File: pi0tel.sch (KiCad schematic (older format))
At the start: 3 parts

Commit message: hmmm
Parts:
- added C1: 680uF, Capacitor_SMD:C_1206_3216Metric_Pad1.42x1.75mm_HandSolder, symbol Device:CP
- added C2: 220uF, Capacitor_SMD:C_1206_3216Metric_Pad1.42x1.75mm_HandSolder, symbol Device:CP
- added D1: Schottky 3A, Diode_SMD:D_1206_3216Metric_Pad1.42x1.75mm_HandSolder, symbol Device:D_Schottky
- added J1: DIN-5_180degree, footprints:din_5_econet_pcb_mount, symbol Connector:DIN-5_180degree
- added J2: RPi_GPIO, Connector_PinHeader_2.54mm:PinHeader_2x20_P2.54mm_Vertical, symbol Connector-ML:RPi_GPIO
- added L1: 33uH, Inductor_SMD:L_12x12mm_H6mm, symbol Device:L
- added U1: LM2596S-5, Package_TO_SOT_SMD:TO-263-5_TabPin3, symbol Regulator_Switching:LM2596S-5
- gave numbers to parts that had none: 2
- renumbered 10k to 10k1
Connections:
- net labels added: GND
- wire segments 13 -> 36
- no-connect marks 0 -> 36
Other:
- note added: "Thru-Hole Connector"
- moved on the sheet: 10k1, Q1, R1

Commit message: grrr
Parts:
- J1: footprint footprints:din_5_econet_pcb_mount -> myelin-kicad:din_5_econet_pcb_mount
- R2: renamed from 10k1; value R -> 10k
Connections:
- net GND: no longer C1.1, J1.5, U1.1 (VIN)
- new net MinitelVcc: C1.1, J1.5, U1.1 (VIN)
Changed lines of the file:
@@
 EESchema Schematic File Version 4
 LIBS:pi0tel-cache
-LIBS:RPi_Zero_pHat_Template-cache
 EELAYER 26 0
 EELAYER END
@@
 $EndComp
 $Comp
-L Device:R 10k1
+L Device:R R2
 U 1 1 5EFD4A91
 P 3200 2600
-F 0 "10k1" H 3270 2646 50  0000 L CNN
-F 1 "R" H 3270 2555 50  0000 L CNN
+F 0 "R2" H 3270 2646 50  0000 L CNN
+F 1 "10k" H 3270 2555 50  0000 L CNN
 F 2 "Resistor_SMD:R_0805_2012Metric_Pad1.15x1.40mm_HandSolder" V 3130 2600 50  0001 C CNN
 F 3 "~" H 3200 2600 50  0001 C CNN
@@
 	1350 4300 1650 4300
 Wire Wire Line
-	1350 4300 1350 4900
-Wire Wire Line
-	1350 4900 1650 4900
-Wire Wire Line
 	2750 4900 2750 4700
-Connection ~ 1350 4300
 Wire Wire Line
 	1650 4750 1650 4900
-Connection ~ 1650 4900
 Wire Wire Line
 	1650 4900 2250 4900
@@
 Wire Wire Line
 	4850 4300 4850 4500
-Text Label 1350 4000 0    50   ~ 0
+Text Label 1350 4300 0    50   ~ 0
 MinitelVcc
-Wire Wire Line
-	1350 4000 1350 4300
 $Comp
 L Connector:DIN-5_180degree J1
@@
 F 0 "J1" H 5500 2526 50  0000 C CNN
 F 1 "DIN-5_180degree" H 5500 2435 50  0000 C CNN
-F 2 "footprints:din_5_econet_pcb_mount" H 5500 2800 50  0001 C CNN
+F 2 "myelin-kicad:din_5_econet_pcb_mount" H 5500 2800 50  0001 C CNN
 F 3 "http://www.mouser.com/ds/2/18/40_c091_abd_e-75918.pdf" H 5500 2800 50  0001 C CNN
 	1    5500 2800

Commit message: hmmm
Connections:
- net +3V3: now also J2.17 (3.3V); no longer J2.1 (3.3V)
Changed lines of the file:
@@
 NoConn ~ 7300 3300
 NoConn ~ 7300 3400
-NoConn ~ 7300 3500
+NoConn ~ 7300 2700
 NoConn ~ 7300 3600
 NoConn ~ 7300 3700
@@
 L power:+3.3V #PWR0107
 U 1 1 5EFA719F
-P 7300 2700
-F 0 "#PWR0107" H 7300 2550 50  0001 C CNN
-F 1 "+3.3V" V 7315 2828 50  0000 L CNN
-F 2 "" H 7300 2700 50  0001 C CNN
-F 3 "" H 7300 2700 50  0001 C CNN
-	1    7300 2700
+P 7300 3500
+F 0 "#PWR0107" H 7300 3350 50  0001 C CNN
+F 1 "+3.3V" V 7315 3628 50  0000 L CNN
+F 2 "" H 7300 3500 50  0001 C CNN
+F 3 "" H 7300 3500 50  0001 C CNN
+	1    7300 3500
 	0    -1   -1   0
 $EndComp

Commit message: getting there
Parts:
- C1: value 680uF -> 270uF; footprint Capacitor_SMD:C_1206_3216Metric_Pad1.42x1.75mm_HandSolder -> Capacitor_SMD:CP_Elec_8x10.5
- C2: value 220uF -> 470uF; footprint Capacitor_SMD:C_1206_3216Metric_Pad1.42x1.75mm_HandSolder -> Capacitor_SMD:CP_Elec_8x10.5
- L1: value 33uH -> 68uH
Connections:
- net +5V: now also J2.4 (5V)
- net GND: now also J2.9 (GND); no longer J2.25 (GND)
- no-connect marks 36 -> 35
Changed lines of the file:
@@
 P 4350 4500
 F 0 "L1" V 4172 4500 50  0000 C CNN
-F 1 "33uH" V 4263 4500 50  0000 C CNN
+F 1 "68uH" V 4263 4500 50  0000 C CNN
 F 2 "Inductor_SMD:L_12x12mm_H6mm" H 4350 4500 50  0001 C CNN
 F 3 "~" H 4350 4500 50  0001 C CNN
@@
 P 1650 4600
 F 0 "C1" H 1768 4646 50  0000 L CNN
-F 1 "680uF" H 1768 4555 50  0000 L CNN
-F 2 "Capacitor_SMD:C_1206_3216Metric_Pad1.42x1.75mm_HandSolder" H 1688 4450 50  0001 C CNN
+F 1 "270uF" H 1768 4555 50  0000 L CNN
+F 2 "Capacitor_SMD:CP_Elec_8x10.5" H 1688 4450 50  0001 C CNN
 F 3 "~" H 1650 4600 50  0001 C CNN
 	1    1650 4600
@@
 P 4850 4700
 F 0 "C2" H 4968 4746 50  0000 L CNN
-F 1 "220uF" H 4968 4655 50  0000 L CNN
-F 2 "Capacitor_SMD:C_1206_3216Metric_Pad1.42x1.75mm_HandSolder" H 4888 4550 50  0001 C CNN
+F 1 "470uF" H 4968 4655 50  0000 L CNN
+F 2 "Capacitor_SMD:CP_Elec_8x10.5" H 4888 4550 50  0001 C CNN
 F 3 "~" H 4850 4700 50  0001 C CNN
 	1    4850 4700
@@
 NoConn ~ 7300 2800
 NoConn ~ 7300 2900
-NoConn ~ 7300 3100
+NoConn ~ 7300 3900
 NoConn ~ 7300 3200
 NoConn ~ 7300 3300
@@
 NoConn ~ 9200 3200
 NoConn ~ 9200 2900
-NoConn ~ 9200 2800
 $Comp
 L power:+5V #PWR0106
@@
 L power:GND #PWR0108
 U 1 1 5EFA81A2
-P 7300 3900
-F 0 "#PWR0108" H 7300 3650 50  0001 C CNN
-F 1 "GND" V 7305 3772 50  0000 R CNN
-F 2 "" H 7300 3900 50  0001 C CNN
-F 3 "" H 7300 3900 50  0001 C CNN
-	1    7300 3900
+P 7300 3100
+F 0 "#PWR0108" H 7300 2850 50  0001 C CNN
+F 1 "GND" V 7305 2972 50  0000 R CNN
+F 2 "" H 7300 3100 50  0001 C CNN
+F 3 "" H 7300 3100 50  0001 C CNN
+	1    7300 3100
 	0    1    1    0
 $EndComp
@@
 Text Label 5800 2700 0    50   ~ 0
 MinitelVcc
+$Comp
+L power:+5V #PWR?
+U 1 1 5EFBBFDE
+P 9200 2800
+F 0 "#PWR?" H 9200 2650 50  0001 C CNN
+F 1 "+5V" V 9215 2928 50  0000 L CNN
+F 2 "" H 9200 2800 50  0001 C CNN
+F 3 "" H 9200 2800 50  0001 C CNN
+	1    9200 2800
+	0    1    1    0
+$EndComp
 $EndSCHEMATC

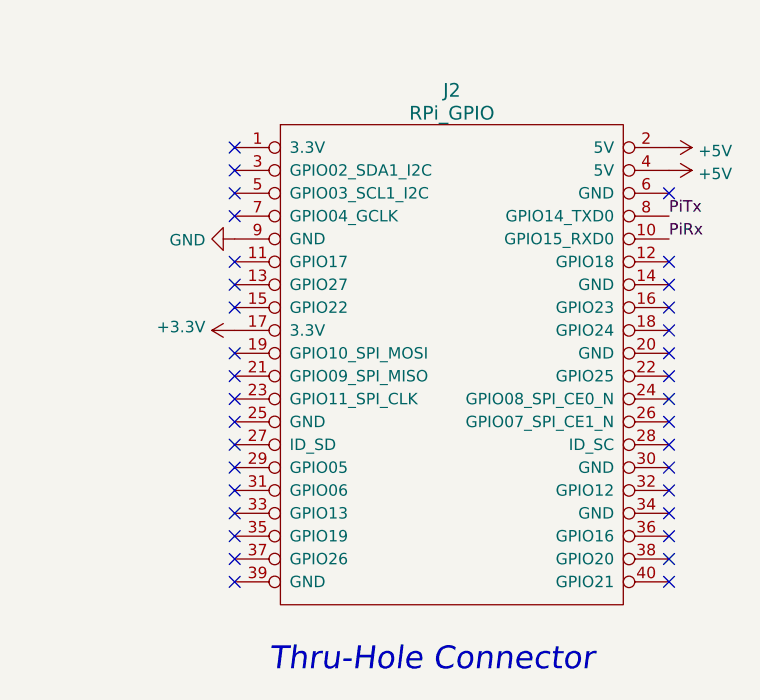
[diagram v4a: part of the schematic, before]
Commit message: Move din to the back
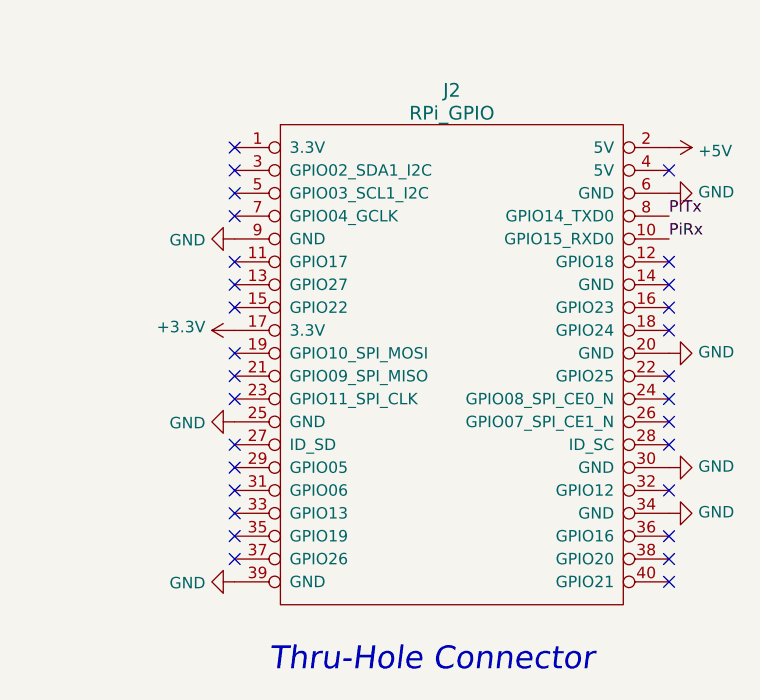
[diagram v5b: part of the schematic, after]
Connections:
- net +5V: no longer J2.4 (5V)
- net GND: now also J2.20 (GND), J2.25 (GND), J2.30 (GND), J2.34 (GND), J2.39 (GND), J2.6 (GND)
- no-connect marks 35 -> 30
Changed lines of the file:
@@
 NoConn ~ 7300 2800
 NoConn ~ 7300 2900
-NoConn ~ 7300 3900
 NoConn ~ 7300 3200
 NoConn ~ 7300 3300
@@
 NoConn ~ 7300 4400
 NoConn ~ 7300 4500
-NoConn ~ 7300 4600
 NoConn ~ 9200 4600
 NoConn ~ 9200 4500
 NoConn ~ 9200 4400
-NoConn ~ 9200 4300
 NoConn ~ 9200 4200
-NoConn ~ 9200 4100
 NoConn ~ 9200 4000
 NoConn ~ 9200 3900
 NoConn ~ 9200 3800
 NoConn ~ 9200 3700
-NoConn ~ 9200 3600
 NoConn ~ 9200 3500
 NoConn ~ 9200 3400
 NoConn ~ 9200 3300
 NoConn ~ 9200 3200
-NoConn ~ 9200 2900
 $Comp
 L power:+5V #PWR0106
@@
 Text Label 5800 2700 0    50   ~ 0
 MinitelVcc
+NoConn ~ 9200 2800
 $Comp
-L power:+5V #PWR?
-U 1 1 5EFBBFDE
-P 9200 2800
-F 0 "#PWR?" H 9200 2650 50  0001 C CNN
-F 1 "+5V" V 9215 2928 50  0000 L CNN
-F 2 "" H 9200 2800 50  0001 C CNN
-F 3 "" H 9200 2800 50  0001 C CNN
-	1    9200 2800
+L power:GND #PWR?
+U 1 1 5EFCD1E8
+P 7300 3900
+F 0 "#PWR?" H 7300 3650 50  0001 C CNN
+F 1 "GND" V 7305 3772 50  0000 R CNN
+F 2 "" H 7300 3900 50  0001 C CNN
+F 3 "" H 7300 3900 50  0001 C CNN
+	1    7300 3900
 	0    1    1    0
 $EndComp
+$Comp
+L power:GND #PWR?
+U 1 1 5EFCD6C1
+P 7300 4600
+F 0 "#PWR?" H 7300 4350 50  0001 C CNN
+F 1 "GND" V 7305 4472 50  0000 R CNN
+F 2 "" H 7300 4600 50  0001 C CNN
+F 3 "" H 7300 4600 50  0001 C CNN
+	1    7300 4600
+	0    1    1    0
+$EndComp
+$Comp
+L power:GND #PWR?
+U 1 1 5EFCE70C
+P 9200 3600
+F 0 "#PWR?" H 9200 3350 50  0001 C CNN
+F 1 "GND" V 9205 3472 50  0000 R CNN
+F 2 "" H 9200 3600 50  0001 C CNN
+F 3 "" H 9200 3600 50  0001 C CNN
+	1    9200 3600
+	0    -1   -1   0
+$EndComp
+$Comp
+L power:GND #PWR?
+U 1 1 5EFCEF5F
+P 9200 4100
+F 0 "#PWR?" H 9200 3850 50  0001 C CNN
+F 1 "GND" V 9205 3972 50  0000 R CNN
+F 2 "" H 9200 4100 50  0001 C CNN
+F 3 "" H 9200 4100 50  0001 C CNN
+	1    9200 4100
+	0    -1   -1   0
+$EndComp
+$Comp
+L power:GND #PWR?
+U 1 1 5EFCEF7E
+P 9200 4300
+F 0 "#PWR?" H 9200 4050 50  0001 C CNN
+F 1 "GND" V 9205 4172 50  0000 R CNN
+F 2 "" H 9200 4300 50  0001 C CNN
+F 3 "" H 9200 4300 50  0001 C CNN
+	1    9200 4300
+	0    -1   -1   0
+$EndComp
+$Comp
+L power:GND #PWR?
+U 1 1 5EFCEFA7
+P 9200 2900
+F 0 "#PWR?" H 9200 2650 50  0001 C CNN
+F 1 "GND" V 9205 2772 50  0000 R CNN
+F 2 "" H 9200 2900 50  0001 C CNN
+F 3 "" H 9200 2900 50  0001 C CNN
+	1    9200 2900
+	0    -1   -1   0
+$EndComp
 $EndSCHEMATC

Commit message: Fix footprint for Schottky
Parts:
- D1: footprint Diode_SMD:D_1206_3216Metric_Pad1.42x1.75mm_HandSolder -> Diode_SMD:D_SMA_Handsoldering
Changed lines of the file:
@@
 F 0 "D1" V 3854 4779 50  0000 L CNN
 F 1 "Schottky 3A" V 3945 4779 50  0000 L CNN
-F 2 "Diode_SMD:D_1206_3216Metric_Pad1.42x1.75mm_HandSolder" H 3900 4700 50  0001 C CNN
+F 2 "Diode_SMD:D_SMA_Handsoldering" H 3900 4700 50  0001 C CNN
 F 3 "~" H 3900 4700 50  0001 C CNN
 	1    3900 4700

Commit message: Enlarge inductance pads for handsolder
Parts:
- L1: footprint Inductor_SMD:L_12x12mm_H6mm -> Inductor_SMD:L_1210_3225Metric_Pad1.42x2.65mm_HandSolder
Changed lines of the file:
@@
 F 0 "L1" V 4172 4500 50  0000 C CNN
 F 1 "68uH" V 4263 4500 50  0000 C CNN
-F 2 "Inductor_SMD:L_12x12mm_H6mm" H 4350 4500 50  0001 C CNN
+F 2 "Inductor_SMD:L_1210_3225Metric_Pad1.42x2.65mm_HandSolder" H 4350 4500 50  0001 C CNN
 F 3 "~" H 4350 4500 50  0001 C CNN
 	1    4350 4500
